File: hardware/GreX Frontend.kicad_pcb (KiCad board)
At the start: 4 copper layers, 88 x 70 mm, 237 parts, among them J1 Conn_Coaxial, J2 Conn_Coaxial, J3 Screw_Terminal_01x04, J4 PROG, J5 Conn_Coaxial, J6 Conn_Coaxial, J7 Conn_Coaxial, U1 PAT1220-C-3DB, U10 COS358SR, U11 TC4-19G2, U12 BAT-15-099R, U13 ADL5611, U14 HMC624A, U15 ADL5611, U16 TMP100, U17 ADL5611, U18 ADL5611, U19 ADL5611, U2 PAT1220-C-3DB, U20 HMC624A, U21 ADL5611, U22 AD8314, U23 TC4-19G2, U24 TC4-19G2, U25 BAT-15-099R, U26 TC4-19G2, U27 AD8314, U28 DSA_Logo, U3 XC6206PxxxMR, U4 AMS1117-5.0, U5 SPX3819M5-L, U6 RP2040, U7 SPX3819M5-L, U8 INA3221, U9 IS25LP080D-JULE, Y1 2TJ412000NYGBC

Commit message: FEM v3 Updates
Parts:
- removed C16: 100n, Capacitor_SMD:C_0402_1005Metric
- removed Ref**: Val**, Library:GReX_pcb
- removed TP1, TP2, TP3, TP4: TestPoint, TestPoint:TestPoint_Pad_D1.0mm
- removed U16: TMP100, Package_TO_SOT_SMD:SOT-23-6
- C105, C33: value 100n -> 470n; footprint Capacitor_SMD:C_0402_1005Metric -> Capacitor_SMD:C_0603_1608Metric
- C21, C22, C23: moved to F.Cu
- L1, L25, L4, L6: value 150u -> 47u; footprint Inductor_SMD:L_1812_4532Metric -> Inductor_SMD:L_0603_1608Metric
- R18, R38: value 28.5 -> 28
- R3, R36: value 225 -> 226
- moved U28 25.6 mm to (114.0, 112.5)
- moved C27 6.68 mm to (175.8, 100.7), turned to 180 degrees
- moved R34 4.50 mm to (165.5, 102.6), turned to 90 degrees
- moved L25 3.74 mm to (110.2, 126.9)
- moved C21 3.67 mm to (170.3, 104.4), turned to -90 degrees
- moved L4 3.51 mm to (110.2, 82.6)
- moved L6 3.11 mm to (110.2, 128.6)
- moved L1 3.06 mm to (110.2, 84.2)
- moved C23 2.33 mm to (171.3, 104.4), turned to -90 degrees
- moved C22 2.19 mm to (169.1, 104.9), turned to 90 degrees
- moved C26 0.72 mm to (168.4, 98.2)
- moved C33 0.65 mm to (107.1, 82.6)
- moved C105 0.25 mm to (107.1, 126.9)
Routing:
- net +5VA: track 294.5 -> 69.7 mm, vias 15 -> 16
- net Net-(U3-VI): track 82.4 -> 16.2 mm, vias 5 -> 6
- net +3V3: track 123.7 -> 80.5 mm, vias 15 -> 10
- net TXD: track 33.7 -> 45.5 mm, vias 2 -> 0
- net CAL_TONE_2: track 40.2 -> 49.7 mm
- net RXD: track 32.6 -> 42.1 mm, vias 2 -> 0
- net MOSI: track 76.4 -> 67.3 mm, vias 4 -> 3
- net VLNA2_-: track 84.3 -> 75.7 mm, vias 3 -> 2
- net CLK: track 75.7 -> 67.6 mm, vias 4 -> 3
- net CAL_TONE_1: track 35.7 -> 43.1 mm
- net SCL: track 19.9 -> 14.0 mm, vias 1 -> 0
- net Net-(C33-Pad2): track 6.71 -> 11.5 mm
- net Net-(C105-Pad2): track 6.71 -> 11.0 mm
- net SDA: track 16.4 -> 12.3 mm, vias 2 -> 0
- net Net-(C105-Pad1): track 5.61 -> 1.54 mm
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- added copper zone on In2.Cu, net +3V3
- added copper zone on In2.Cu, net +5VA
- added copper zone on In2.Cu, net Net-(U3-VI)
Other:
- board text added: "FEM - Rev 3 K. Shila"
- board text added: "{ "ViaStitching": "0.1", "stitch_zone_0": { "HSpacing": "1", "VSpacing": "1", "Clearance": "0", "Randomize": false } }"
- board text added: "{ "ViaStitching": "0.1", "stitch_zone_0": { "HSpacing": "10", "VSpacing": "10", "Clearance": "1", "Randomize": false } }"
- board text added: "{ "ViaStitching": "0.1", "stitch_zone_0": { "HSpacing": "3", "VSpacing": "3", "Clearance": "0", "Randomize": false } }"
- board text added: "{ "ViaStitching": "0.1", "stitch_zone_0": { "HSpacing": "5", "VSpacing": "5", "Clearance": "0", "Randomize": false } }"
- board text removed: "FEM - Rev 2 K. Shila"

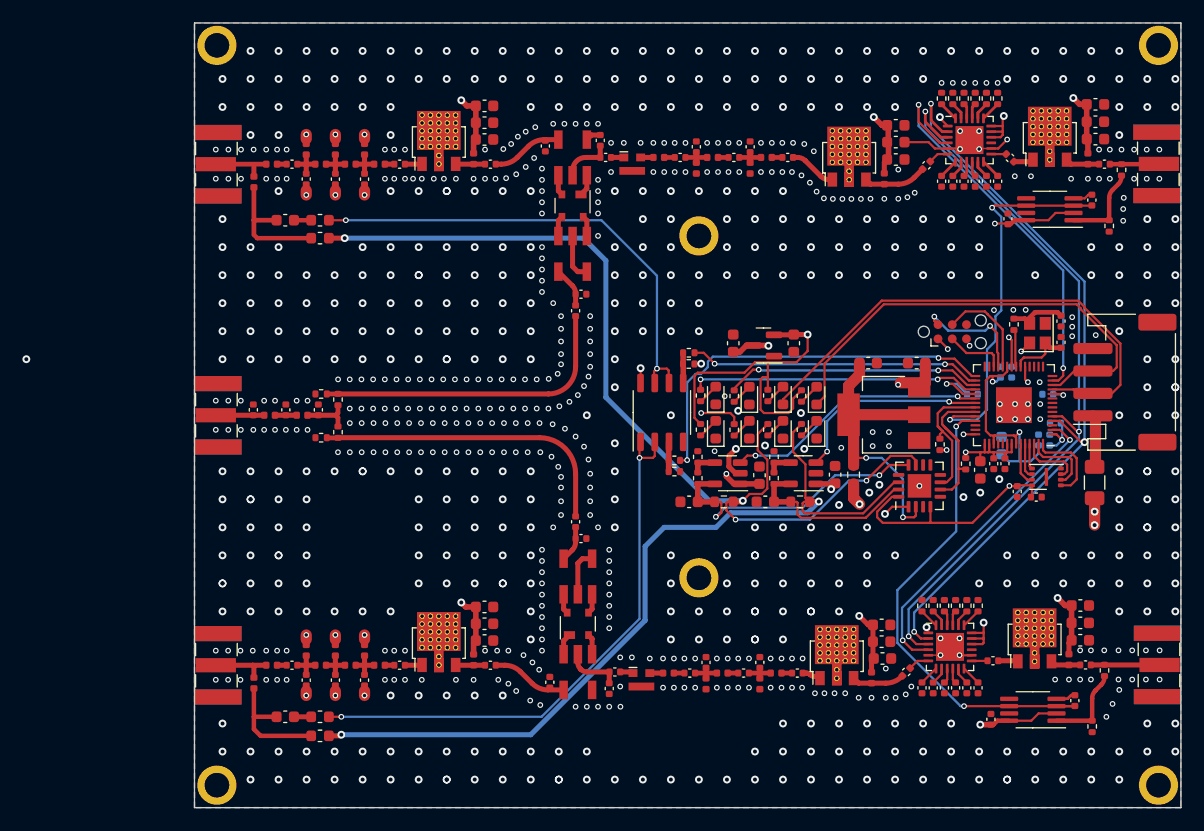
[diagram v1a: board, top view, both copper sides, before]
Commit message: Remove cal circuit, swap attens, swap norflash
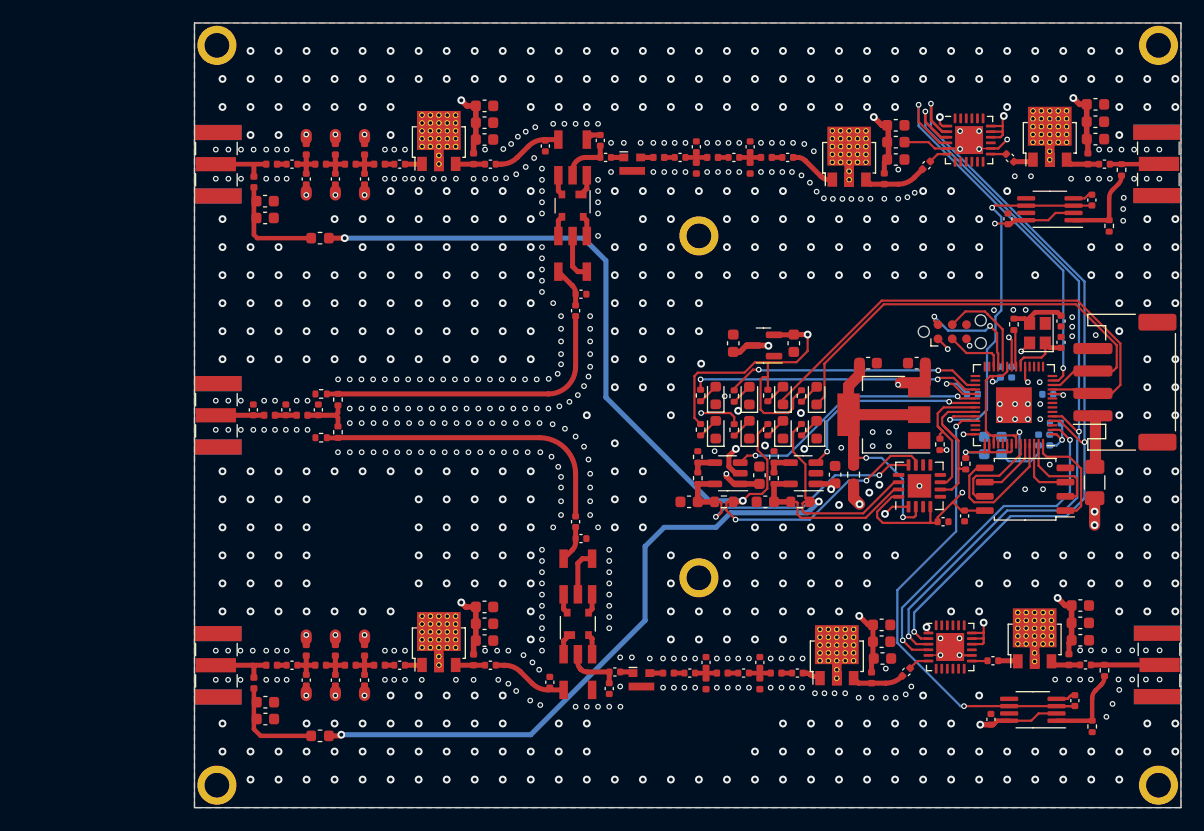
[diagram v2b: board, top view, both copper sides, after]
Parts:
- removed C105: 470n, Capacitor_SMD:C_0603_1608Metric
- removed C21, C23, C48, C50, C51, C52, C53, C55, C78, C79, C80, C81, C82, C83: 100n, Capacitor_SMD:C_0402_1005Metric
- removed L25, L4: 47u, Inductor_SMD:L_0603_1608Metric
- removed R17, R19, R20, R21, R26, R27, R28, R29, R30, R31, R32, R33, R37, R39, R40, R41: 10k, Resistor_SMD:R_0402_1005Metric
- removed U10: COS358SR, Package_SO:SOP-8_3.9x4.9mm_P1.27mm
- removed U20: HMC624A, Package_CSP:LFCSP-24-1EP_4x4mm_P0.5mm_EP2.5x2.5mm
- added C101: 1.2n, Capacitor_SMD:C_0603_1608Metric, F.Cu at (105.3, 127.1)
- added C102: 68p, Capacitor_SMD:C_0603_1608Metric, F.Cu at (105.3, 125.6)
- added C16: 1.2n, Capacitor_SMD:C_0603_1608Metric, F.Cu at (105.3, 80.9)
- added U16: HMC1122, Package_CSP:LFCSP-24-1EP_4x4mm_P0.5mm_EP2.5x2.5mm, F.Cu at (166.4, 120.7)
- C22: moved to B.Cu
- C33: value 470n -> 68p
- U14: value HMC624A -> HMC1122
- U9: value IS25LP080D-JULE -> IS25LP080D-JBLE; footprint Library:USON-8-1EP_3x2mm_P0.5mm_EP0.2x1.6mm -> Package_SO:SOIC-8_5.275x5.275mm_P1.27mm
- moved C17 7.15 mm to (165.8, 109.5), turned to 0 degrees
- moved C15 6.62 mm to (167.7, 109.0), turned to -90 degrees
- moved C22 2.20 mm to (169.4, 102.7), turned to -90 degrees
- moved U9 2.20 mm to (173.1, 106.6)
- moved C33 1.81 mm to (105.3, 82.4)
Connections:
- C33 pad 1: Net-(C33-Pad1) -> GND
- U14 pad 10: Net-(U14-ACG4) -> GND
- U14 pad 11: Net-(U14-ACG5) -> GND
- U14 pad 12: Net-(U14-ACG6) -> GND
- U14 pad 19: Net-(U14-D5) -> GND
- U14 pad 20: Net-(U14-D4) -> GND
- U14 pad 21: Net-(U14-D3) -> GND
- U14 pad 22: Net-(U14-D2) -> GND
- U14 pad 23: Net-(U14-D1) -> GND
- U14 pad 24: Net-(U14-D0) -> GND
- U14 pad 7: Net-(U14-ACG1) -> GND
- U14 pad 8: Net-(U14-ACG2) -> GND
- U14 pad 9: Net-(U14-ACG3) -> GND
- U6 pad 29: RF2_32kHz -> unconnected-(U6-GPIO18-Pad29)
- U6 pad 30: RF1_32kHz -> unconnected-(U6-GPIO19-Pad30)
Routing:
- net CAL_TONE_2: track 49.7 -> 0.00 mm, vias 2 -> 0
- net CAL_TONE_1: track 43.1 -> 0.00 mm, vias 2 -> 0
- net RF2_32kHz: track 34.9 -> 0.00 mm, vias 2 -> 0
- net RF1_32kHz: track 26.1 -> 0.00 mm, vias 2 -> 0
- net Net-(U6-QSPI_SD0): track 2.30 -> 11.8 mm
- net Net-(U6-QSPI_SD3): track 3.88 -> 8.55 mm
- net +3V3: track 80.5 -> 75.9 mm
- net MOSI: track 67.3 -> 70.2 mm
- net CLK: track 67.6 -> 70.5 mm
- net ATTEN_LE_2: track 28.7 -> 31.4 mm
- net Net-(U10-+IN2): track 2.67 -> 0.00 mm
- net Net-(U6-QSPI_SCLK): track 3.15 -> 5.80 mm
- net Net-(U10-+IN1): track 2.62 -> 0.00 mm
- net Net-(U6-QSPI_SS): track 7.41 -> 9.73 mm
- net Net-(C16-Pad2): track 11.5 -> 9.47 mm
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
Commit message: Update FEM hardware design for production version
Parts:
- renumbered C16 to C1, C14 to C10, C15 to C11, C97 to C12, C17 to C13, C98 to C14, C18 to C15, C19 to C16, C20 to C17, C24 to C18, C22 to C19, C33 to C2, C25 to C20, C26 to C21, C27 to C22, C28 to C23, C29 to C24, C30 to C25, C31 to C26, C32 to C27, C34 to C28, C39 to C29, C2 to C3, C37 to C30, C41 to C31, C42 to C32, C44 to C33, C45 to C34, C46 to C35, C47 to C36, C63 to C37, C58 to C38, C59 to C39, C7 to C4, C56 to C40, C66 to C41, C61 to C42, C62 to C43, C64 to C44, C65 to C45, C67 to C46, C4 to C47, C11 to C48, C70 to C49, C8 to C5, C71 to C50, C72 to C51, C101 to C52, C102 to C53, C74 to C54, C75 to C55, C76 to C56, C77 to C57, C49 to C58, C86 to C59, C9 to C6, C87 to C60, C84 to C61, C54 to C62, C89 to C63, C90 to C64, C91 to C65, C43 to C66, C68 to C67, C69 to C68, C92 to C69, C10 to C7, C93 to C70, C94 to C71, C95 to C72, C96 to C73, C1 to C74, C5 to C75, C6 to C76, C38 to C77, C40 to C78, C57 to C79, C12 to C8, C60 to C80, C73 to C81, C85 to C82, C88 to C83, C3 to C84, C35 to C85, C36 to C86, C99 to C87, C100 to C88, C13 to C9, H4 to H1, H5 to H2, H6 to H3, H1 to H4, H2 to H5, H3 to H6, J3 to J2, J4 to J3, J7 to J4, J2 to J5, J5 to J6, J6 to J7, L16 to L10, L17 to L11, L18 to L12, L20 to L13, L21 to L14, L13 to L15, L14 to L16, L22 to L17, L23 to L18, L29 to L19, L30 to L20, L31 to L21, L6 to L22, L24 to L23, L26 to L24, L10 to L25, L27 to L26, L28 to L27, L32 to L28, L33 to L29, L5 to L3, L34 to L30, L35 to L31, L36 to L32, L37 to L33, L38 to L34, L3 to L35, L8 to L36, L7 to L4, L9 to L5, L11 to L6, L12 to L7, L15 to L8, L19 to L9, R44 to R16, R34 to R17, R35 to R18, R22 to R19, R23 to R20, R24 to R21, R25 to R22, R3 to R23, R18 to R24, R36 to R25, R38 to R26, R4 to R3, R5 to R4, R6 to R5, R7 to R6, R16 to R7, U28 to U1, U1 to U10, U13 to U11, U14 to U12, U15 to U13, U19 to U14, U16 to U15, U21 to U16, U24 to U17, U25 to U18, U26 to U19, U3 to U2, U17 to U20, U18 to U21, U11 to U23, U12 to U24, U23 to U25, U27 to U26, U4 to U3, U5 to U4, U7 to U5, U8 to U6, U9 to U7, U6 to U8, U2 to U9
